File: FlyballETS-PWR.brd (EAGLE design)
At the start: 39.4 x 50.8 mm, 9 parts

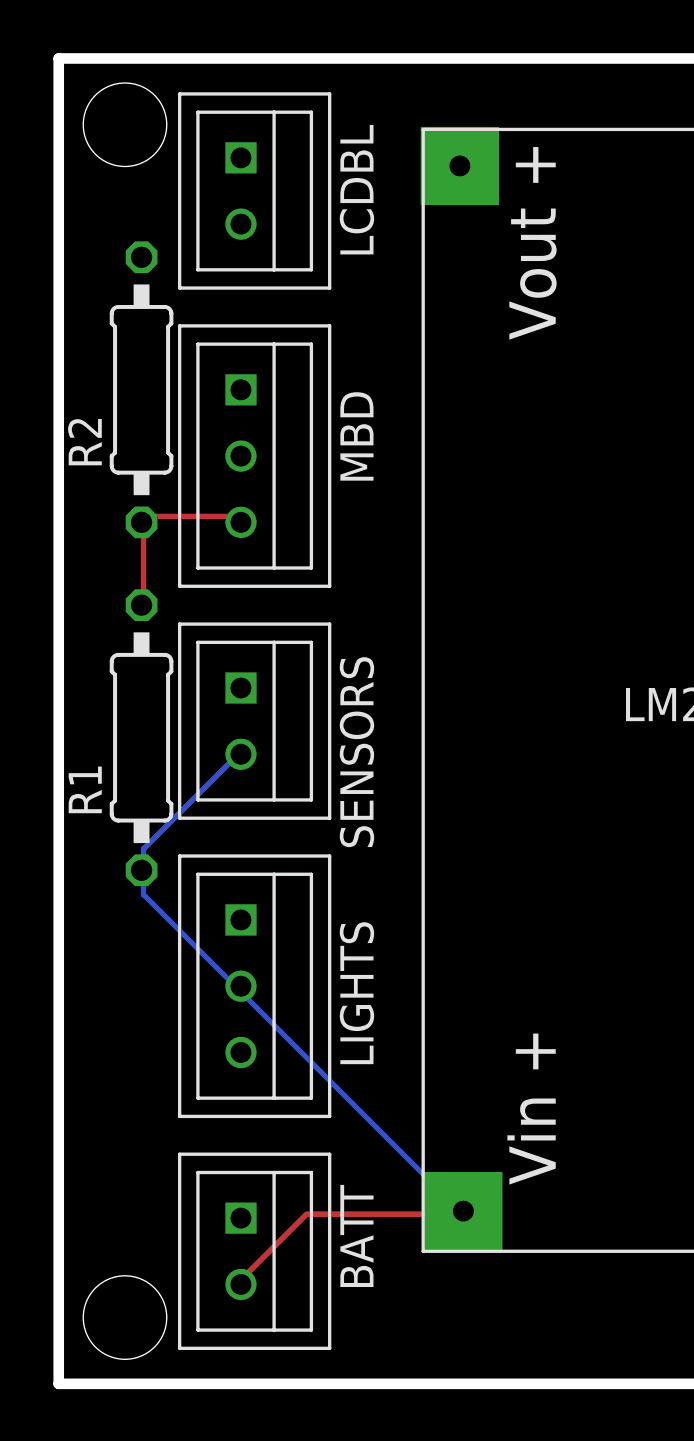
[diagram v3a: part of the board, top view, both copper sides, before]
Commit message: Fixed several issues
- Checked all mounting holes (fixes #1 )
- Marked light colors on lights PCB (fixes #7 )
- Swapped pins 2 and 3 on LIGHTS connected on PWR board (fixes #3 )
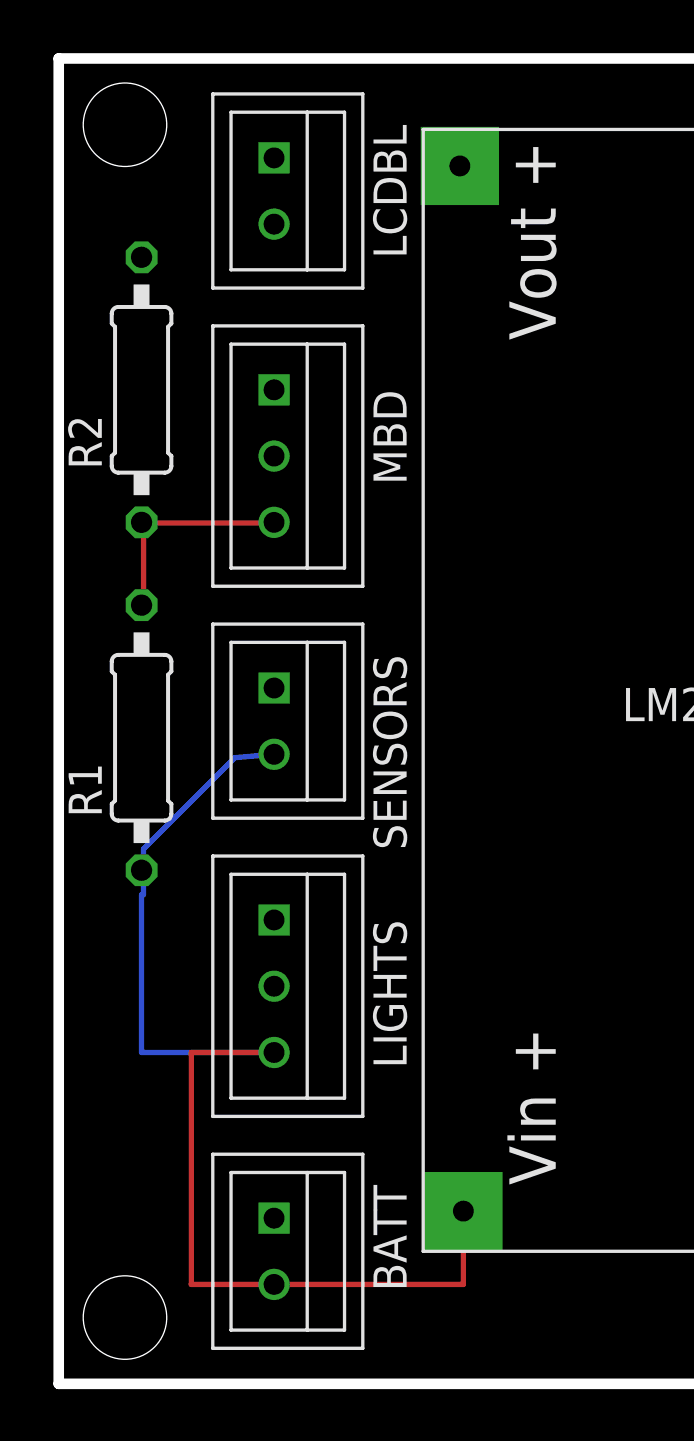
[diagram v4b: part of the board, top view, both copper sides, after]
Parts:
- moved BATT 1.27 mm to (8.26, 3.81)
- moved LCDBL 1.27 mm to (8.26, 44.5)
- moved LIGHTS 1.27 mm to (8.26, 15.2)
- moved MBD 1.27 mm to (8.26, 35.6)
- moved SENSORS 1.27 mm to (8.26, 24.1)
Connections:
- net +12V: now also LIGHTS.P$3; no longer LIGHTS.P$2
- net +5V: now also LIGHTS.P$2; no longer LIGHTS.P$3
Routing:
- net +12V: track 34.4 -> 44.8 mm
- net N$1: track 7.32 -> 8.29 mm
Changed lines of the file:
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@@
 </class>
 </classes>
-<designrules name="LaenPCBOrder">
+<designrules name="oshpark-2layer">
 <description language="de">&lt;b&gt;EAGLE Design Rules&lt;/b&gt;
 &lt;p&gt;
@@
 <param name="mvStopFrame" value="1"/>
 <param name="mvCreamFrame" value="0"/>
-<param name="mlMinStopFrame" value="3mil"/>
-<param name="mlMaxStopFrame" value="3mil"/>
+<param name="mlMinStopFrame" value="2.5mil"/>
+<param name="mlMaxStopFrame" value="2.5mil"/>
 <param name="mlMinCreamFrame" value="0mil"/>
 <param name="mlMaxCreamFrame" value="0mil"/>
@@
 </autorouter>
 <elements>
-<element name="BATT" library="bt_con-jst-xh" package="B2B-XH" value="02-JST-B2B-XH-A" x="6.985" y="3.81" smashed="yes" rot="R270">
-<attribute name="NAME" x="10.795" y="7.62" size="1.27" layer="21" rot="R270"/>
-</element>
-<element name="LCDBL" library="bt_con-jst-xh" package="B2B-XH" value="02-JST-B2B-XH-A" x="6.985" y="44.45" smashed="yes" rot="R270">
-<attribute name="NAME" x="10.795" y="48.26" size="1.27" layer="21" rot="R270"/>
-</element>
-<element name="LIGHTS" library="bt_con-jst-xh" package="B3B-XH" value="03-JST-B3B-XH-A" x="6.985" y="15.24" smashed="yes" rot="R270">
-<attribute name="NAME" x="10.795" y="17.78" size="1.27" layer="21" rot="R270"/>
-</element>
-<element name="MBD" library="bt_con-jst-xh" package="B3B-XH" value="03-JST-B3B-XH-A" x="6.985" y="35.56" smashed="yes" rot="R270">
-<attribute name="NAME" x="10.795" y="38.1" size="1.27" layer="21" rot="R270"/>
+<element name="BATT" library="bt_con-jst-xh" package="B2B-XH" value="02-JST-B2B-XH-A" x="8.255" y="3.81" smashed="yes" rot="R270">
+<attribute name="NAME" x="12.065" y="7.62" size="1.27" layer="21" rot="R270"/>
+</element>
+<element name="LCDBL" library="bt_con-jst-xh" package="B2B-XH" value="02-JST-B2B-XH-A" x="8.255" y="44.45" smashed="yes" rot="R270">
+<attribute name="NAME" x="12.065" y="48.26" size="1.27" layer="21" rot="R270"/>
+</element>
+<element name="LIGHTS" library="bt_con-jst-xh" package="B3B-XH" value="03-JST-B3B-XH-A" x="8.255" y="15.24" smashed="yes" rot="R270">
+<attribute name="NAME" x="12.065" y="17.78" size="1.27" layer="21" rot="R270"/>
+</element>
+<element name="MBD" library="bt_con-jst-xh" package="B3B-XH" value="03-JST-B3B-XH-A" x="8.255" y="35.56" smashed="yes" rot="R270">
+<attribute name="NAME" x="12.065" y="38.1" size="1.27" layer="21" rot="R270"/>
 </element>
 <element name="R1" library="resistor" package="0207/10" value="5.6k" x="3.175" y="24.765" rot="R90"/>
 <element name="R2" library="resistor" package="0207/10" value="3.9k" x="3.175" y="38.1" rot="R90"/>
-<element name="SENSORS" library="bt_con-jst-xh" package="B2B-XH" value="02-JST-B2B-XH-A" x="6.985" y="24.13" smashed="yes" rot="R270">
-<attribute name="NAME" x="10.795" y="27.94" size="1.27" layer="21" rot="R270"/>
+<element name="SENSORS" library="bt_con-jst-xh" package="B2B-XH" value="02-JST-B2B-XH-A" x="8.255" y="24.13" smashed="yes" rot="R270">
+<attribute name="NAME" x="12.065" y="27.94" size="1.27" layer="21" rot="R270"/>
 </element>
 <element name="U$1" library="_custom" package="LM2596-BOARD" value="LM2596-BOARD" x="13.97" y="5.08"/>
@@
 <signals>
 <signal name="+5V">
-<contactref element="LIGHTS" pad="P$3"/>
 <contactref element="MBD" pad="P$2"/>
 <contactref element="LCDBL" pad="P$2"/>
@@
 </polygon>
 <contactref element="U$1" pad="VOUT"/>
+<contactref element="LIGHTS" pad="P$2"/>
 </signal>
 <signal name="GND">
@@
 <contactref element="BATT" pad="P$2"/>
 <contactref element="SENSORS" pad="P$2"/>
-<contactref element="LIGHTS" pad="P$2"/>
 <contactref element="R1" pad="1"/>
 <contactref element="U$1" pad="VIN"/>
-<wire x1="3.25" y1="18.75" x2="6.75" y2="15.25" width="0.2032" layer="16"/>
 <wire x1="3.25" y1="19.5" x2="3.25" y2="18.75" width="0.2032" layer="16"/>
-<wire x1="6.75" y1="15.25" x2="6.985" y2="15.24" width="0.2032" layer="16"/>
 <wire x1="3.25" y1="19.5" x2="3.175" y2="19.685" width="0.2032" layer="16"/>
 <wire x1="3.25" y1="20.5" x2="6.75" y2="24" width="0.2032" layer="16"/>
 <wire x1="3.25" y1="19.75" x2="3.25" y2="20.5" width="0.2032" layer="16"/>
-<wire x1="6.75" y1="24" x2="6.985" y2="24.13" width="0.2032" layer="16"/>
+<wire x1="6.75" y1="24" x2="8.255" y2="24.13" width="0.2032" layer="16"/>
 <wire x1="3.25" y1="19.75" x2="3.175" y2="19.685" width="0.2032" layer="16"/>
-<wire x1="9.5" y1="6.5" x2="7" y2="4" width="0.2032" layer="1"/>
-<wire x1="15.5" y1="6.5" x2="9.5" y2="6.5" width="0.2032" layer="1"/>
-<wire x1="7" y1="4" x2="6.985" y2="3.81" width="0.2032" layer="1"/>
-<wire x1="15.5" y1="6.5" x2="15.51" y2="6.62" width="0.2032" layer="1"/>
-<wire x1="15.5" y1="6.5" x2="7" y2="15" width="0.2032" layer="16"/>
-<wire x1="7" y1="15" x2="6.985" y2="15.24" width="0.2032" layer="16"/>
-<wire x1="15.5" y1="6.5" x2="15.51" y2="6.62" width="0.2032" layer="16"/>
+<contactref element="LIGHTS" pad="P$3"/>
+<wire x1="8.255" y1="12.7" x2="5.08" y2="12.7" width="0.2032" layer="1"/>
+<wire x1="5.08" y1="12.7" x2="5.08" y2="3.81" width="0.2032" layer="1"/>
+<wire x1="5.08" y1="3.81" x2="8.255" y2="3.81" width="0.2032" layer="1"/>
+<wire x1="3.25" y1="18.75" x2="3.175" y2="18.75" width="0.2032" layer="16"/>
+<wire x1="3.175" y1="18.75" x2="3.175" y2="12.7" width="0.2032" layer="16"/>
+<wire x1="3.175" y1="12.7" x2="8.255" y2="12.7" width="0.2032" layer="16"/>
+<wire x1="8.255" y1="3.81" x2="15.51" y2="3.81" width="0.2032" layer="1"/>
+<wire x1="15.51" y1="3.81" x2="15.51" y2="6.62" width="0.2032" layer="1"/>
 </signal>
 <signal name="N$1">
@@
 <contactref element="R2" pad="1"/>
 <contactref element="MBD" pad="P$3"/>
-<wire x1="3.25" y1="33.25" x2="6.75" y2="33.25" width="0.2032" layer="1"/>
-<wire x1="6.75" y1="33.25" x2="6.985" y2="33.02" width="0.2032" layer="1"/>
-<wire x1="3.25" y1="33.25" x2="3.175" y2="33.02" width="0.2032" layer="1"/>
 <wire x1="3.25" y1="33" x2="3.25" y2="30" width="0.2032" layer="1"/>
 <wire x1="3.25" y1="30" x2="3.175" y2="29.845" width="0.2032" layer="1"/>
-<wire x1="3.25" y1="33" x2="3.175" y2="33.02" width="0.2032" layer="1"/>
+<wire x1="3.25" y1="33" x2="8.255" y2="33" width="0.2032" layer="1"/>
+<wire x1="8.255" y1="33" x2="8.255" y2="33.02" width="0.2032" layer="1"/>
+<wire x1="3.25" y1="33" x2="3.175" y2="33" width="0.2032" layer="1"/>
+<wire x1="3.175" y1="33" x2="3.175" y2="33.02" width="0.2032" layer="1"/>
 </signal>
 </signals>

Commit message: Fixed JST XH pin numbering
Updated bt_con-jst-xh.lbr library with swapped pin numbering.
Updated all board designs with updated library so they have the
connectors the right way around
Fixes #4
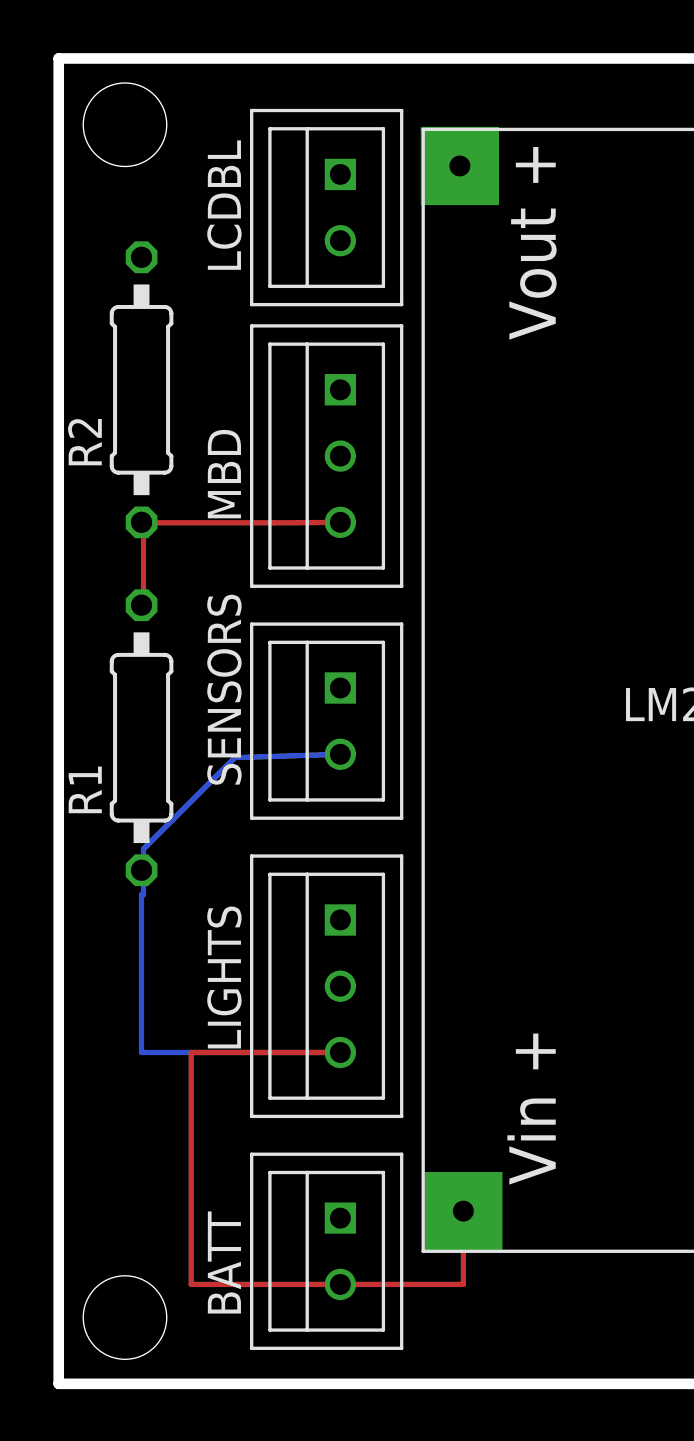
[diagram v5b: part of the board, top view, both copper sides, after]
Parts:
- BATT, LCDBL, SENSORS: value 02-JST-B2B-XH-A -> 02-JST
- moved LCDBL 2.62 mm to (10.8, 43.8), turned to 90 degrees
- moved BATT 2.54 mm to (10.8, 3.81), turned to 90 degrees
- moved LIGHTS 2.54 mm to (10.8, 15.2), turned to 90 degrees
- moved MBD 2.54 mm to (10.8, 35.6), turned to 90 degrees
- moved SENSORS 2.54 mm to (10.8, 24.1), turned to 90 degrees
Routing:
- net +12V: track 44.8 -> 52.4 mm
- net N$1: track 8.29 -> 10.8 mm
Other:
- board text added: "FlyballETS PowerBoard v3 http://bit.ly/2hV18aC LICENSE: CC-BY-SA"
- board text removed: "FlyballETS PowerBoard v2 http://bit.ly/1ErZ5QD LICENSE: CC-BY-SA"
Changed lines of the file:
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@@
 <?xml version="1.0" encoding="utf-8"?>
 <!DOCTYPE eagle SYSTEM "eagle.dtd">
-<eagle version="7.5.0">
+<eagle version="8.2.2">
 <drawing>
 <settings>
@@
 <hole x="36.83" y="2.54" drill="3.2"/>
 <text x="19.05" y="15.24" size="1.778" layer="22" rot="MR90">FlyballETS
-PowerBoard v2
-http://bit.ly/1ErZ5QD
+PowerBoard v3
+http://bit.ly/2hV18aC
 LICENSE: CC-BY-SA</text>
 <text x="77.47" y="-27.94" size="2.54" layer="48">Alex Goris</text>
 <text x="25.4" y="-40.64" size="2.54" layer="48">FlyballETS
-PowerBoard v2
-http://bit.ly/1ErZ5QD
+PowerBoard v3
+http://bit.ly/2hV18aC
 LICENSE: CC-BY-SA</text>
 <dimension x1="39.37" y1="0" x2="39.37" y2="50.8" x3="44.449996875" y3="25.4" textsize="1.778" layer="48"/>
@@
 </autorouter>
 <elements>
-<element name="BATT" library="bt_con-jst-xh" package="B2B-XH" value="02-JST-B2B-XH-A" x="8.255" y="3.81" smashed="yes" rot="R270">
-<attribute name="NAME" x="12.065" y="7.62" size="1.27" layer="21" rot="R270"/>
-</element>
-<element name="LCDBL" library="bt_con-jst-xh" package="B2B-XH" value="02-JST-B2B-XH-A" x="8.255" y="44.45" smashed="yes" rot="R270">
-<attribute name="NAME" x="12.065" y="48.26" size="1.27" layer="21" rot="R270"/>
-</element>
-<element name="LIGHTS" library="bt_con-jst-xh" package="B3B-XH" value="03-JST-B3B-XH-A" x="8.255" y="15.24" smashed="yes" rot="R270">
-<attribute name="NAME" x="12.065" y="17.78" size="1.27" layer="21" rot="R270"/>
-</element>
-<element name="MBD" library="bt_con-jst-xh" package="B3B-XH" value="03-JST-B3B-XH-A" x="8.255" y="35.56" smashed="yes" rot="R270">
-<attribute name="NAME" x="12.065" y="38.1" size="1.27" layer="21" rot="R270"/>
-</element>
-<element name="R1" library="resistor" package="0207/10" value="5.6k" x="3.175" y="24.765" rot="R90"/>
-<element name="R2" library="resistor" package="0207/10" value="3.9k" x="3.175" y="38.1" rot="R90"/>
-<element name="SENSORS" library="bt_con-jst-xh" package="B2B-XH" value="02-JST-B2B-XH-A" x="8.255" y="24.13" smashed="yes" rot="R270">
-<attribute name="NAME" x="12.065" y="27.94" size="1.27" layer="21" rot="R270"/>
+<element name="BATT" library="bt_con-jst-xh" package="B2B-XH" value="02-JST" x="10.795" y="3.81" smashed="yes" rot="R90">
+<attribute name="NAME" x="6.985" y="2.54" size="1.27" layer="21" rot="R90"/>
+</element>
+<element name="LCDBL" library="bt_con-jst-xh" package="B2B-XH" value="02-JST" x="10.795" y="43.815" smashed="yes" rot="R90">
+<attribute name="NAME" x="6.985" y="42.545" size="1.27" layer="21" rot="R90"/>
+</element>
+<element name="LIGHTS" library="bt_con-jst-xh" package="B3B-XH" value="03-JST-B3B-XH-A" x="10.795" y="15.24" smashed="yes" rot="R90">
+<attribute name="NAME" x="6.985" y="12.7" size="1.27" layer="21" rot="R90"/>
+</element>
+<element name="MBD" library="bt_con-jst-xh" package="B3B-XH" value="03-JST-B3B-XH-A" x="10.795" y="35.56" smashed="yes" rot="R90">
+<attribute name="NAME" x="6.985" y="33.02" size="1.27" layer="21" rot="R90"/>
+</element>
+<element name="R1" library="resistor" library_urn="urn:adsk.eagle:library:348" package="0207/10" value="5.6k" x="3.175" y="24.765" rot="R90"/>
+<element name="R2" library="resistor" library_urn="urn:adsk.eagle:library:348" package="0207/10" value="3.9k" x="3.175" y="38.1" rot="R90"/>
+<element name="SENSORS" library="bt_con-jst-xh" package="B2B-XH" value="02-JST" x="10.795" y="24.13" smashed="yes" rot="R90">
+<attribute name="NAME" x="6.985" y="22.86" size="1.27" layer="21" rot="R90"/>
 </element>
 <element name="U$1" library="_custom" package="LM2596-BOARD" value="LM2596-BOARD" x="13.97" y="5.08"/>
-<element name="U$2" library="frames" package="A5L-LOC" value="" x="-63.5" y="-48.26"/>
+<element name="U$2" library="frames" library_urn="urn:adsk.eagle:library:229" package="A5L-LOC" value="" x="-63.5" y="-48.26"/>
 </elements>
 <signals>
@@
 <wire x1="3.25" y1="20.5" x2="6.75" y2="24" width="0.2032" layer="16"/>
 <wire x1="3.25" y1="19.75" x2="3.25" y2="20.5" width="0.2032" layer="16"/>
-<wire x1="6.75" y1="24" x2="8.255" y2="24.13" width="0.2032" layer="16"/>
+<wire x1="6.75" y1="24" x2="10.795" y2="24.13" width="0.2032" layer="16"/>
 <wire x1="3.25" y1="19.75" x2="3.175" y2="19.685" width="0.2032" layer="16"/>
 <contactref element="LIGHTS" pad="P$3"/>
-<wire x1="8.255" y1="12.7" x2="5.08" y2="12.7" width="0.2032" layer="1"/>
+<wire x1="10.795" y1="12.7" x2="5.08" y2="12.7" width="0.2032" layer="1"/>
 <wire x1="5.08" y1="12.7" x2="5.08" y2="3.81" width="0.2032" layer="1"/>
-<wire x1="5.08" y1="3.81" x2="8.255" y2="3.81" width="0.2032" layer="1"/>
+<wire x1="5.08" y1="3.81" x2="10.795" y2="3.81" width="0.2032" layer="1"/>
 <wire x1="3.25" y1="18.75" x2="3.175" y2="18.75" width="0.2032" layer="16"/>
 <wire x1="3.175" y1="18.75" x2="3.175" y2="12.7" width="0.2032" layer="16"/>
-<wire x1="3.175" y1="12.7" x2="8.255" y2="12.7" width="0.2032" layer="16"/>
-<wire x1="8.255" y1="3.81" x2="15.51" y2="3.81" width="0.2032" layer="1"/>
+<wire x1="3.175" y1="12.7" x2="10.795" y2="12.7" width="0.2032" layer="16"/>
+<wire x1="10.795" y1="3.81" x2="15.51" y2="3.81" width="0.2032" layer="1"/>
 <wire x1="15.51" y1="3.81" x2="15.51" y2="6.62" width="0.2032" layer="1"/>
 </signal>
@@
 <wire x1="3.25" y1="30" x2="3.175" y2="29.845" width="0.2032" layer="1"/>
 <wire x1="3.25" y1="33" x2="8.255" y2="33" width="0.2032" layer="1"/>
-<wire x1="8.255" y1="33" x2="8.255" y2="33.02" width="0.2032" layer="1"/>
+<wire x1="8.255" y1="33" x2="10.795" y2="33.02" width="0.2032" layer="1"/>
 <wire x1="3.25" y1="33" x2="3.175" y2="33" width="0.2032" layer="1"/>
 <wire x1="3.175" y1="33" x2="3.175" y2="33.02" width="0.2032" layer="1"/>
@@
 which will not be processed correctly with this version.
 </note>
+<note version="8.2" severity="warning">
+Since Version 8.2, Eagle supports online libraries. The ids
+of those online libraries will not be understood (or retained)
+with this version.
+</note>
 </compatibility>
